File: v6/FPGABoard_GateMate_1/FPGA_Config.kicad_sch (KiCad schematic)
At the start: 14 parts, among them J1 Conn_01x06_Pin, SW1 SW_DIP_x04, U1 CCGM1A1, U2 W25Q16JVUXIQ

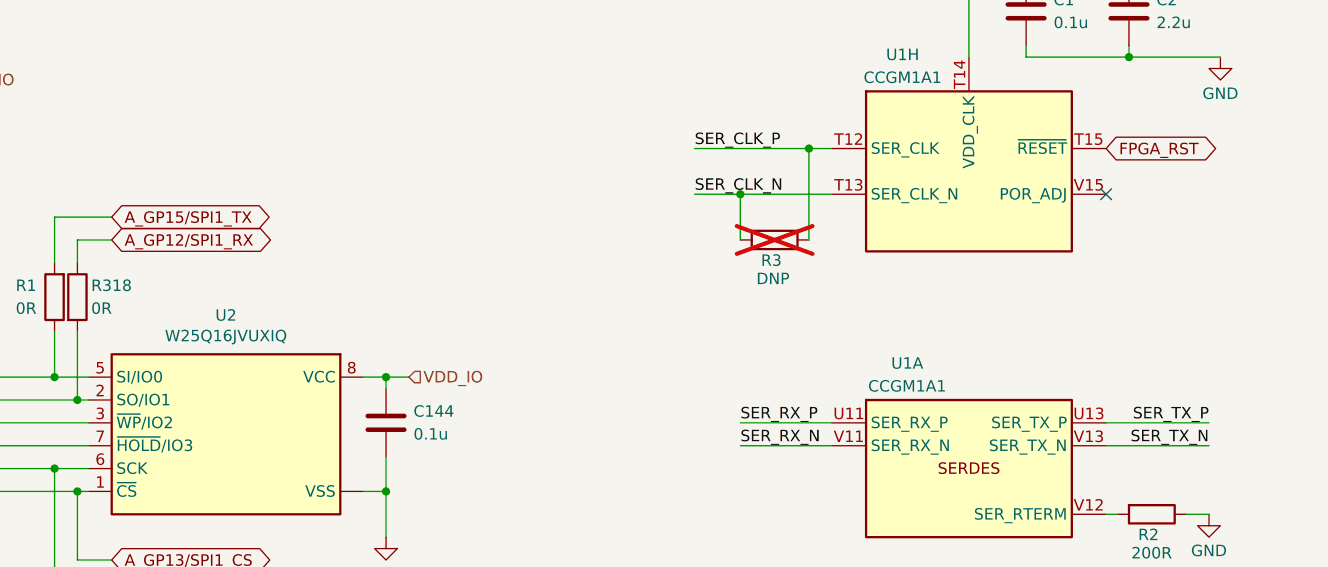
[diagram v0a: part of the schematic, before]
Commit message: Add comments for GateMAte board
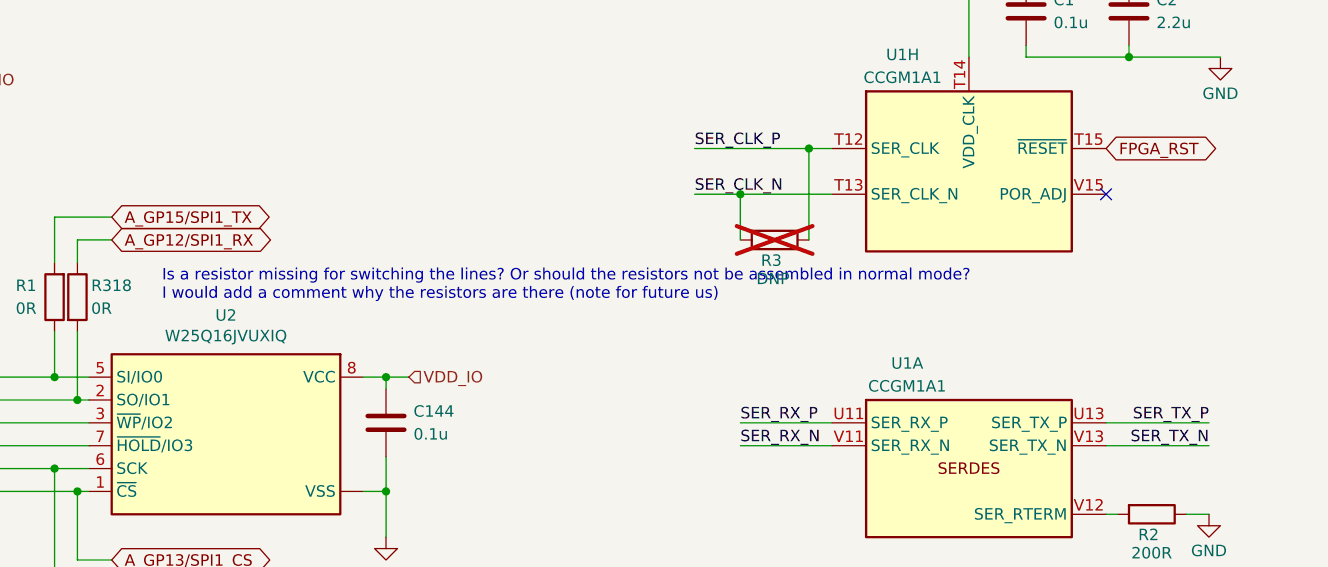
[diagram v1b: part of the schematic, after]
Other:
- note added: "Is a resistor missing for switching the lines? Or should the resistors not be assembled in normal mode? I would add a comment why the resistors are there (note for future us)"
